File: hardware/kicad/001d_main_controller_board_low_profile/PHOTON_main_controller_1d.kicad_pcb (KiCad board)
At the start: 2 copper layers, 54 x 49.9 mm, 65 parts, among them J101 JST_SH, J102 JST_SH RS-485_1, J103 JST_SH RS-485_2, J104 JST_SH RS-485_2, J3 USB_C_Receptacle_USB2.0, J4 Micro_SD_Card, U1 RP2354_60QFN, U102 THVD1424RGTR, U4 TPD4E05U06DQAR, U5 TPS62A0569ADRLR, Y1 ABM8-272-T3

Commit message: 002 sensor board: 5V bus rework, library consolidation, DRC pass
Board (002):
- Remove SS14 bridging diode; USB-C VBUS and JST V+ are now one net.
  Worst case is back-powering a host's VBUS, acceptable in a uniform
  5V fleet, and it drops 185mW in the bridging case.
- Remove the 8x 47k CS pull-ups. At 47k they parked the TLA2518 CS
  inputs mid-rail (1.7-2.1V, between VIL 0.99 and VIH 2.31); the
  internal pull-down now defines them cleanly low. Firmware must drive
  CS high before configuring SPI.
- 5V pour along the bottom edge, 3.3V moved up to the mounting rail.
- USB-C relocated; ~200mm D+/D- run on F.Cu over the B.Cu GND pour.
- Screw-head keepouts on all mounting holes.
- Board grown 2mm in Y -> 413.66 x 35.00 mm.

Net classes:
- USB_DIFF_90 -> USB_FS, diff pair 0.8/0.15 -> 0.35/0.15. The old name
  claimed 90 ohm; on a 1.51mm 2-layer stackup it is ~140 ohm and cannot
  be otherwise. Irrelevant at Full Speed.
- Add PWR_5V (+5V) and RS485 (/RS485_P, /RS485_N).
- Restore the +3V3 -> VCC assignment lost during the rename.

Libraries:
- footprints/ -> footprints.pretty/ so KiCad will save into it.
- Consolidate symbols into PHOTON / PHOTON_Modified on 001d and 002;
  drop unused vendor-exported libraries.
- Add mousebite_34mm: 17x 1.2mm NPTH at 2mm pitch. 0.8mm webs cut more
  easily than the old 1.4mm and still pass a 0.3mm trace.
- Fix MountingHole_2.7mm_M2.5_Keepout: it disallowed pads, so each hole
  flagged its own NPTH (17 DRC errors).

Fab outputs now tracked via .gitignore negation for production/*.csv.

Co-Authored-By: Claude Opus 5 <noreply@anthropic.com>
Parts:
- G***: footprint SparkFun-Qwiic:qwiic_8mm -> footprints:qwiic_8mm
- J4: footprint Pretty Custom:TF-015_corrected -> footprints:TF-015_corrected
- U102: footprint Pretty Custom:QFN_24RGTR_TEX -> footprints:QFN_24RGTR_TEX
- U4: footprint Pretty Custom:DQA0010A -> footprints:DQA0010A
- U5: footprint Pretty Custom:DRL0006A-MFG -> footprints:SOT-563_DRL0006A
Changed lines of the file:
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@@
 		)
 	)
-	(footprint "Pretty Custom:TF-015_corrected"
+	(footprint "footprints:TF-015_corrected"
 		(layer "F.Cu")
 		(at 50.65 4.235 180)
@@
 		)
 	)
-	(footprint "Pretty Custom:DQA0010A"
+	(footprint "footprints:DQA0010A"
 		(layer "F.Cu")
 		(at 34.349998 38.925 -90)
@@
 		)
 	)
-	(footprint "SparkFun-Qwiic:qwiic_8mm"
+	(footprint "footprints:qwiic_8mm"
 		(layer "F.Cu")
 		(at 33.5 9.08 180)
@@
 		)
 	)
-	(footprint "Pretty Custom:QFN_24RGTR_TEX"
+	(footprint "footprints:QFN_24RGTR_TEX"
 		(layer "F.Cu")
 		(at 59.398389 38.613352 -90)
@@
 		)
 	)
-	(footprint "Pretty Custom:DRL0006A-MFG"
+	(footprint "footprints:SOT-563_DRL0006A"
 		(layer "F.Cu")
 		(at 24.03 40.299999 90)
@@
 			)
 		)
-		(property ki_fp_filters "DRL0006A-MFG")
+		(property ki_fp_filters "SOT-563*")
 		(sheetname "/")
 		(sheetfile "PHOTON_main_controller_1d.kicad_sch")

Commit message: Consolidate footprints into a single shared library
All three boards carried their own copies of the same footprints - 79
files across 11 project libraries for 37 distinct footprints. Several
existed three times over (RP2350-QFN-60 ThermalVias, edge_holes,
TO-236_VIS-L, SON_NT2020_VIS, L_pol_2016, USB_Micro-B). Three copies
drift, and this project has already been bitten twice by a library and
a board disagreeing.

- New hardware/kicad/common.pretty holds all 37, verified byte-identical
  where they were duplicated: zero name collisions with differing
  content, so nothing had to be reconciled.
- Each board's fp-lib-table is now a single "common" entry. Previously
  001 alone had eight, and the nickname "footprints" meant a different
  library on each of the three boards - so lib_ids were rewritten per
  board, not globally.
- 459 footprint references across the three boards now resolve. That
  includes SparkFun-Qwiic:qwiic_8mm on 001, which was referenced but
  had never been in any fp-lib-table - broken before this change.

Also shrinks docs/images/reflective_sensor.png from 2816x1536 / 4.43 MB
to 1600x873 / 1.72 MB.

Co-Authored-By: Claude Opus 5 <noreply@anthropic.com>
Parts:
- C2, C3: footprint RP2350_60QFN_minimal:C_0402_1005Metric_small_pads -> common:C_0402_1005Metric_small_pads
- G***: footprint footprints:qwiic_8mm -> common:qwiic_8mm
- J4: footprint footprints:TF-015_corrected -> common:TF-015_corrected
- L1: footprint RP2350_60QFN_minimal:L_pol_2016 -> common:L_pol_2016
- U1: footprint RP2350_60QFN_minimal:RP2350-QFN-60-1EP_7x7_P0.4mm_EP3.4x3.4mm_ThermalVias -> common:RP2350-QFN-60-1EP_7x7_P0.4mm_EP3.4x3.4mm_ThermalVias
- U102: footprint footprints:QFN_24RGTR_TEX -> common:QFN_24RGTR_TEX
- U4: footprint footprints:DQA0010A -> common:DQA0010A
- U5: footprint footprints:SOT-563_DRL0006A -> common:SOT-563_DRL0006A
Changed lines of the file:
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@@
 		)
 	)
-	(footprint "footprints:TF-015_corrected"
+	(footprint "common:TF-015_corrected"
 		(layer "F.Cu")
 		(at 50.65 4.235 180)
@@
 		(embedded_fonts no)
 	)
-	(footprint "RP2350_60QFN_minimal:RP2350-QFN-60-1EP_7x7_P0.4mm_EP3.4x3.4mm_ThermalVias"
+	(footprint "common:RP2350-QFN-60-1EP_7x7_P0.4mm_EP3.4x3.4mm_ThermalVias"
 		(layer "F.Cu")
 		(at 34.765 25.97 180)
@@
 		)
 	)
-	(footprint "footprints:DQA0010A"
+	(footprint "common:DQA0010A"
 		(layer "F.Cu")
 		(at 34.349998 38.925 -90)
@@
 		)
 	)
-	(footprint "RP2350_60QFN_minimal:C_0402_1005Metric_small_pads"
+	(footprint "common:C_0402_1005Metric_small_pads"
 		(layer "F.Cu")
 		(at 32.695 30.61 180)
@@
 		)
 	)
-	(footprint "footprints:qwiic_8mm"
+	(footprint "common:qwiic_8mm"
 		(layer "F.Cu")
 		(at 33.5 9.08 180)
@@
 		)
 	)
-	(footprint "RP2350_60QFN_minimal:C_0402_1005Metric_small_pads"
+	(footprint "common:C_0402_1005Metric_small_pads"
 		(layer "F.Cu")
 		(at 32.695 31.59 180)
@@
 		)
 	)
-	(footprint "footprints:QFN_24RGTR_TEX"
+	(footprint "common:QFN_24RGTR_TEX"
 		(layer "F.Cu")
 		(at 59.398389 38.613352 -90)
@@
 		)
 	)
-	(footprint "footprints:SOT-563_DRL0006A"
+	(footprint "common:SOT-563_DRL0006A"
 		(layer "F.Cu")
 		(at 24.03 40.299999 90)
@@
 		(embedded_fonts no)
 	)
-	(footprint "RP2350_60QFN_minimal:L_pol_2016"
+	(footprint "common:L_pol_2016"
 		(layer "F.Cu")
 		(at 32.38 33.16 180)

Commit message: Rename shared footprint library common -> photon_common
'common' is too generic for a library nickname - it can collide with a
global library or another project's table, and it doesn't identify whose
footprints these are.

155 lib_ids rewritten across the three boards plus all three
fp-lib-tables. All 459 footprint references still resolve.

Co-Authored-By: Claude Opus 5 <noreply@anthropic.com>
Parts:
- C2, C3: footprint common:C_0402_1005Metric_small_pads -> photon_common:C_0402_1005Metric_small_pads
- G***: footprint common:qwiic_8mm -> photon_common:qwiic_8mm
- J4: footprint common:TF-015_corrected -> photon_common:TF-015_corrected
- L1: footprint common:L_pol_2016 -> photon_common:L_pol_2016
- U1: footprint common:RP2350-QFN-60-1EP_7x7_P0.4mm_EP3.4x3.4mm_ThermalVias -> photon_common:RP2350-QFN-60-1EP_7x7_P0.4mm_EP3.4x3.4mm_ThermalVias
- U102: footprint common:QFN_24RGTR_TEX -> photon_common:QFN_24RGTR_TEX
- U4: footprint common:DQA0010A -> photon_common:DQA0010A
- U5: footprint common:SOT-563_DRL0006A -> photon_common:SOT-563_DRL0006A
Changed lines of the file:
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@@
 		)
 	)
-	(footprint "common:TF-015_corrected"
+	(footprint "photon_common:TF-015_corrected"
 		(layer "F.Cu")
 		(at 50.65 4.235 180)
@@
 		(embedded_fonts no)
 	)
-	(footprint "common:RP2350-QFN-60-1EP_7x7_P0.4mm_EP3.4x3.4mm_ThermalVias"
+	(footprint "photon_common:RP2350-QFN-60-1EP_7x7_P0.4mm_EP3.4x3.4mm_ThermalVias"
 		(layer "F.Cu")
 		(at 34.765 25.97 180)
@@
 		)
 	)
-	(footprint "common:DQA0010A"
+	(footprint "photon_common:DQA0010A"
 		(layer "F.Cu")
 		(at 34.349998 38.925 -90)
@@
 		)
 	)
-	(footprint "common:C_0402_1005Metric_small_pads"
+	(footprint "photon_common:C_0402_1005Metric_small_pads"
 		(layer "F.Cu")
 		(at 32.695 30.61 180)
@@
 		)
 	)
-	(footprint "common:qwiic_8mm"
+	(footprint "photon_common:qwiic_8mm"
 		(layer "F.Cu")
 		(at 33.5 9.08 180)
@@
 		)
 	)
-	(footprint "common:C_0402_1005Metric_small_pads"
+	(footprint "photon_common:C_0402_1005Metric_small_pads"
 		(layer "F.Cu")
 		(at 32.695 31.59 180)
@@
 		)
 	)
-	(footprint "common:QFN_24RGTR_TEX"
+	(footprint "photon_common:QFN_24RGTR_TEX"
 		(layer "F.Cu")
 		(at 59.398389 38.613352 -90)
@@
 		)
 	)
-	(footprint "common:SOT-563_DRL0006A"
+	(footprint "photon_common:SOT-563_DRL0006A"
 		(layer "F.Cu")
 		(at 24.03 40.299999 90)
@@
 		(embedded_fonts no)
 	)
-	(footprint "common:L_pol_2016"
+	(footprint "photon_common:L_pol_2016"
 		(layer "F.Cu")
 		(at 32.38 33.16 180)

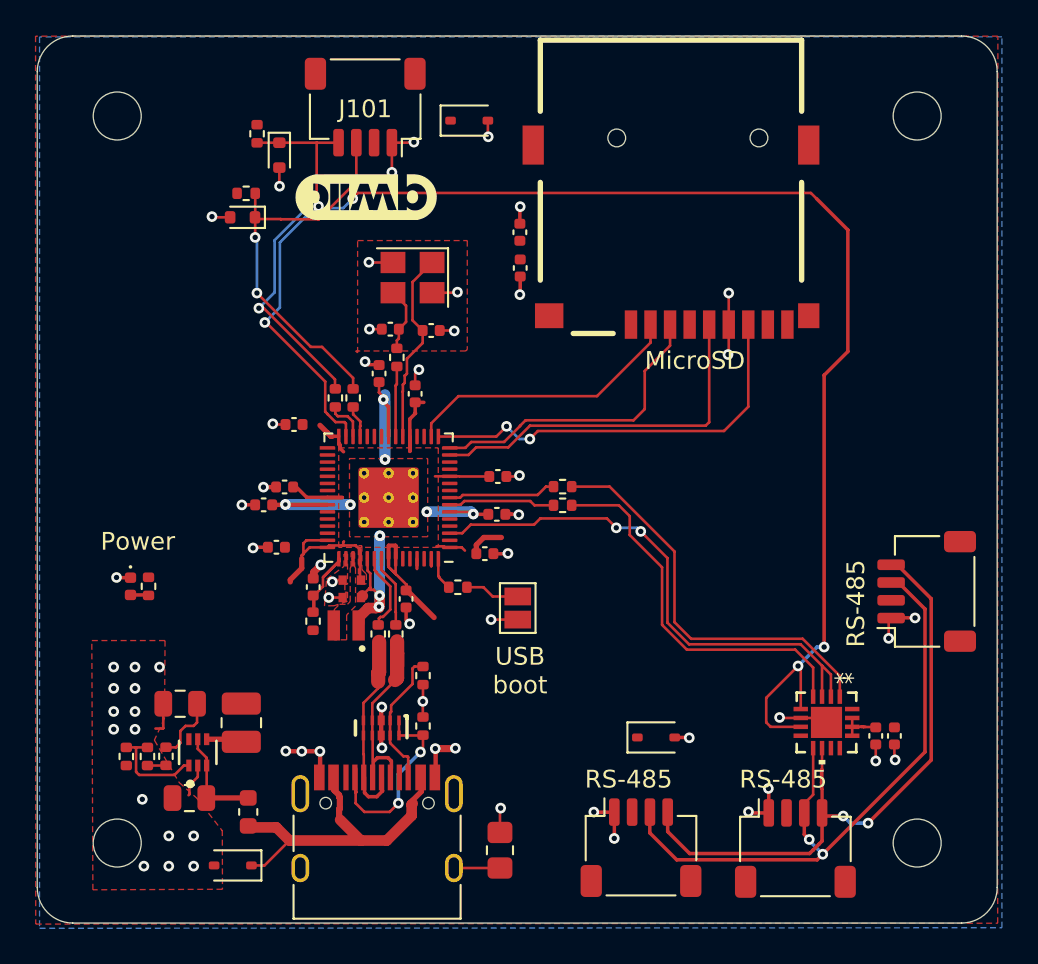
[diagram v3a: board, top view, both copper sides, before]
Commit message: Consolidate symbol libraries, normalise BOM data, Rev B for all three boards
Libraries
- Move PHOTON and PHOTON_Modified to hardware/kicad/, shared by all three
  projects, replacing six divergent per-project copies. 002's versions taken
  as canonical (correct pin electrical types); 001-only parts recovered from
  the schematic cache. All 459 footprint and 464 symbol refs resolve.
- Repoint every sym-lib-table at the shared files. Nicknames unchanged, so
  002 and 001d needed no lib_id edits; only 001's stale date-named ones.
- Fix stale footprint nicknames inside the symbol libraries (footprints:,
  RP2350_60QFN_minimal:, APS6404L-3SQR-ZR:) that would have made newly
  placed parts land with unresolvable footprints.
- Reset baked-in reference designators and MPNs on six library footprints
  back to REF** and the footprint name. SOT-563_DRL0006A carried "U6",
  which would have overwritten 001d's U5 on any field-resetting update.

Footprints
- Add SON-8_3x2mm_P0.5mm: KiCad stock SON-8 with the exposed pad and its
  four paste apertures removed. The APS6404L USON-8L (JEDEC MO-229) has no
  thermal pad and 0-0.05mm standoff, so both the copper and the paste under
  the body were wrong. Replaces the easyeda2kicad footprint on U101, whose
  0.102mm mask margin also bridged all six 0.5mm-pitch mask openings.
- Mounting holes on 001 and 001d move to the photon_common keepout
  footprint, matching 002, so a screw head cannot bridge the F.Cu power
  pour to the B.Cu ground pour.
- Remove the unused TDK T3902 microphone footprint.

BOM
- Normalise values fleet-wide: Greek mu -> ascii u, strip spaces before
  units, complete truncated inductor values. Each was splitting one part
  into two BOM lines, since the fab toolkit groups on footprint+value.
- Unify JST-SH connector values so each board emits one line, not three.
  Per-connector labels moved to Description, which is not a BOM column.
- Assign part numbers to the four largest passive lines: 100nF C1525,
  1uF C52923, 1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
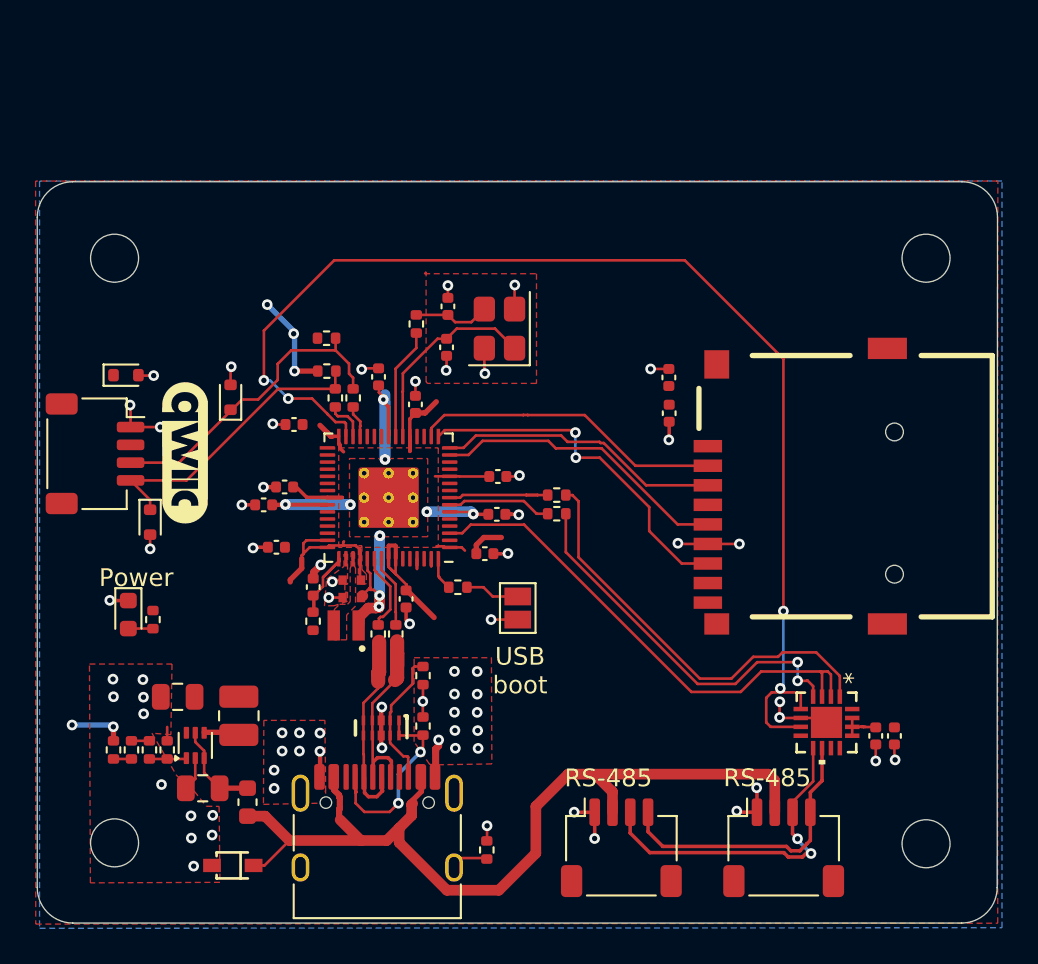
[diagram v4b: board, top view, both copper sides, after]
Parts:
- removed CR101, CR5: H7VHD3UA, Diode_SMD:D_SOD-323
- removed J104: JST_SH RS-485_2, Connector_JST:JST_SH_SM04B-SRSS-TB_1x04-1MP_P1.00mm_Horizontal
- added D12: D_TVS, Diode_SMD:D_SOD-523, F.Cu at (20.0, 19.1)
- added R106: 51kΩ, Resistor_SMD:R_0402_1005Metric, F.Cu at (21.3, 40.2)
- C104, C106: value 1μF -> 1uF
- CR1: value H7VHD3UA -> PTVSHC3D7VU; footprint Diode_SMD:D_SOD-323 -> photon_common:SOD-323_L1.8-W1.3-LS2.5-RD
- D3: value LED GREEN -> LED RED; footprint LED_SMD:LED_0402_1005Metric -> LED_SMD:LED_0603_1608Metric
- H101, H102, H103, H104: footprint MountingHole:MountingHole_2.7mm_M2.5_ISO7380 -> photon_common:MountingHole_2.7mm_M2.5_Keepout
- J102: value JST_SH RS-485_1 -> JST_SH
- J103: value JST_SH RS-485_2 -> JST_SH
- L1: value 3.3u -> 3.3uH
- L2: value 1 uH -> 1uH
- R1: value 1MΩ -> 0Ω; footprint Resistor_SMD:R_0805_2012Metric_Pad1.20x1.40mm_HandSolder -> Resistor_SMD:R_0402_1005Metric
- R104: value 300kΩ -> 200kΩ
- R105: value 150kΩ -> 200kΩ
- R2, R3: value 5.1 kΩ -> 5.1kΩ
- moved J4 25.4 mm to (64.7, 25.3), turned to 90 degrees
- moved J101 24.7 mm to (18.2, 23.5), turned to -90 degrees
- moved D11 21.9 mm to (21.4, 27.4)
- moved G*** 17.6 mm to (23.3, 23.4), turned to -90 degrees
- moved R237 13.9 mm to (31.3, 18.9), turned to 180 degrees
- moved C106 11.7 mm to (50.5, 19.2)
- moved C105 11.7 mm to (50.5, 21.2)
- moved D10 10.1 mm to (25.9, 20.3), turned to 90 degrees
- moved R236 9.32 mm to (31.3, 17.0)
- moved H103 8.02 mm to (65.0, 12.5)
- moved H104 8.00 mm to (19.4, 12.5)
- moved Y1 5.67 mm to (41.0, 16.5), turned to 90 degrees
- moved C18 3.48 mm to (38.1, 15.2), turned to 90 degrees
- moved R104 2.97 mm to (19.3, 40.2), turned to 90 degrees
- moved R103 2.33 mm to (22.3, 40.2), turned to 90 degrees
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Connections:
- CR1 pad 1: VBUS -> +5V
- FB1 pad 1: VBUS -> +5V
- J102 pad 2: +3V3 -> +5V
- J103 pad 2: +3V3 -> +5V
- J3 pad A4: VBUS -> +5V
- J3 pad A9: VBUS -> +5V
- J3 pad B4: VBUS -> +5V
- J3 pad B9: VBUS -> +5V
- R104 pad 1: +3V3 -> Net-(R104-Pad1)
- R104 pad 2: Net-(R104-Pad2) -> +3V3
- R105 pad 1: Net-(R104-Pad2) -> Net-(R105-Pad1)
- R105 pad 2: Net-(U5-FB) -> Net-(R104-Pad1)
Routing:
- net +5V: track 0.00 -> 51.5 mm
- net /RS485_N: track 38.4 -> 15.9 mm, vias 2 -> 0
- net /RS485_P: track 36.9 -> 17.7 mm
- net VBUS: track 19.1 -> 0.00 mm
- net /GPIO18: track 81.9 -> 67.4 mm
- net GND: track 57.5 -> 51.4 mm, vias 62 -> 70
- net +3V3: track 41.8 -> 47.2 mm, vias 0 -> 5
- net /I2C_0_SCL: track 22.1 -> 16.8 mm, vias 2 -> 0
- net /I2C_0_SDA: track 22.3 -> 18.0 mm, vias 2 -> 0
- net /GPIO10: track 20.9 -> 16.8 mm
- net Net-(U5-FB): track 5.66 -> 2.20 mm
- net /GPIO12: track 23.3 -> 20.0 mm
- net /XOUT: track 3.96 -> 6.29 mm
- net /GPIO1: track 30.5 -> 28.8 mm, vias 2 -> 0
- net /GPIO13: track 16.0 -> 17.5 mm
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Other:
- board size 54 x 49.9 mm -> 54 x 41.7 mm
- board text added: "Noah Jaffe A004 REV B"
- board text removed: "MicroSD"
- board text removed: "Noah Jaffe A004 REV A"
